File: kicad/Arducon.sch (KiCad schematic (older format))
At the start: 75 parts, among them J101 To Radio, J102 DB9 Female, J103 To Antenna, J104 Conn_01x08, J105 Conn_01x08, J106 Logic Level, J107 External Power Source, J108 Controlled Power, J109 Conn_01x01, J110 Conn_01x01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

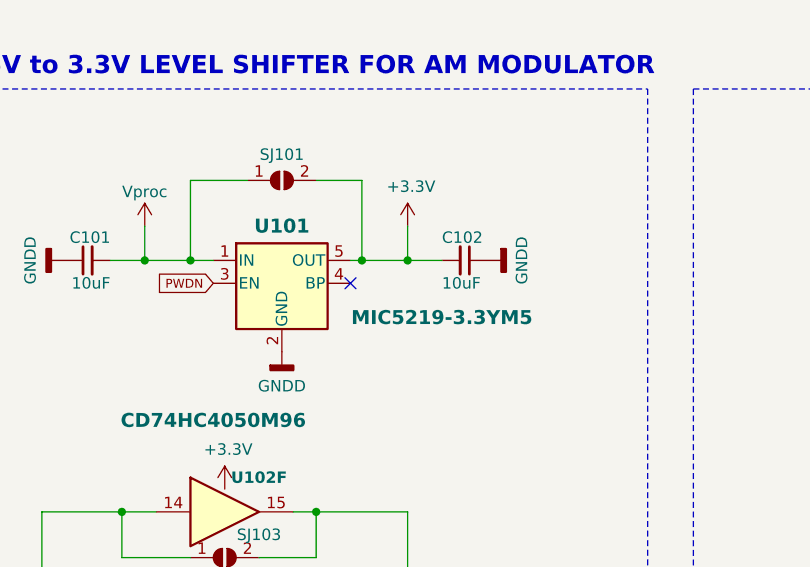
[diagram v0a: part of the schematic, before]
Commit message: PCB Design Updates
Updates for manufacturability. Expanded BOM information items.
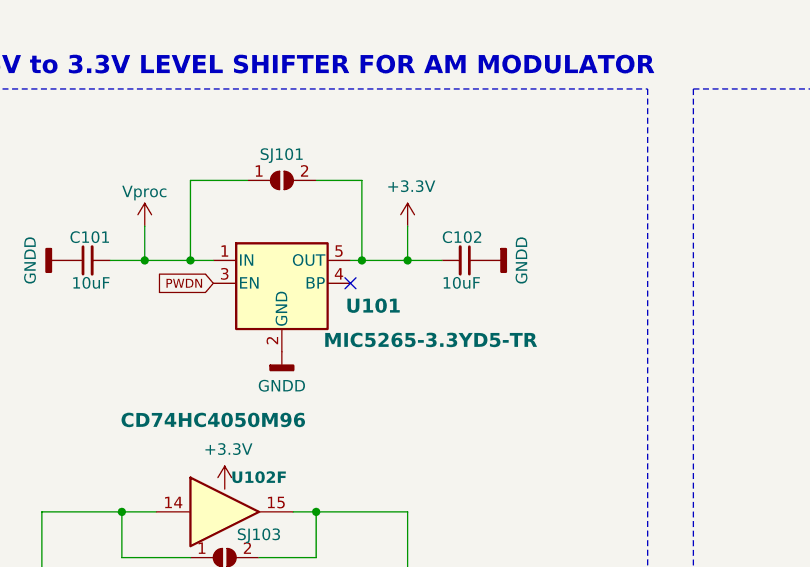
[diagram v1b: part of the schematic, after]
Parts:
- C101, C102, C104: LCSC Part Number (none) -> C15850
- C103, C108, C109, C110: LCSC Part Number (none) -> C476766
- D101, D108, D109: value MSS1P4-M3_89A -> MSS1P2L-M3/89A; Description DIODE SCHOTTKY 40V 1A MICROSMP -> DIODE SCHOTTKY 20V 1A MICROSMP; LCSC Part Number (none) -> C506621; Link <a href=\"https://www.digikey.com/products/en?keywords=MSS1P4-M3/89AGICT-ND\">Link</a> -> <a href=\"https://www.digikey.com/products/en?keywords=MSS1P2L-M3/89AGICT-ND\">Link</a>; Manufacturer PN MSS1P4-M3/89A -> MSS1P2L-M3/89A; Part No. MSS1P4-M3/89AGICT-ND -> MSS1P2L-M3/89AGICT-ND
- D102: LCSC Part Number (none) -> C389523
- D103, D104, D105, D106, D107: LCSC Part Number (none) -> C316054
- FB101, FB102, FB103, FB104, FB105, FB106: LCSC Part Number (none) -> C96697
- Q101, Q103, Q104: LCSC Part Number (none) -> C181121
- Q102: value LMN400E01 -> LMN200; Description MCU LOAD SWITCH 400MA SOT-363 -> MCU LOAD SWITCH 200MA SOT-363; LCSC Part Number (none) -> C150757; Link <a href=\"https://www.digikey.com/products/en?keywords=LMN4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 -> <a href=\"https://www.digikey.com/products/en?keywords=LMN2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; Manufacturer PN LMN400E01-7 -> LMN200B02-7; Part No. LMN400E01DICT-ND -> LMN200B02DICT-ND
- R101, R106: LCSC Part Number (none) -> C96346
- R102: LCSC Part Number (none) -> C114561
- R103, R104, R108, R109, R111, R112: LCSC Part Number (none) -> C17414
- R105: LCSC Part Number (none) -> C107700
- R107: LCSC Part Number (none) -> C416820
- R110: LCSC Part Number (none) -> C193989
- R113: LCSC Part Number (none) -> C170839
- R114: LCSC Part Number (none) -> C328396
- RV101: LCSC Part Number (none) -> C719176
- SW101: LCSC Part Number (none) -> C221877; Manufacturer PN PTS645SL50SMTR92 LFS -> PTS645SL50SMTR92LFS
- SW102: LCSC Part Number (none) -> C221841
- U101: value MIC5219-3.3YM5 -> MIC5265-3.3YD5-TR; Description IC REG LINEAR 3.3V 500MA SOT23-5 -> IC REG LINEAR 3.3V 150MA SOT23-5; LCSC Part Number (none) -> C37970; Link <a href=\"https://www.digikey.com/products/en?keywords=576-1281-1-ND \">Link</a> -> <a href=\"https://www.digikey.com/products/en?keywords=576-2835-1-ND\">Link</a>; Manufacturer PN MIC5219-3.3YM5-TR -> MIC5265-3.3YD5-TR; Part No. 576-1281-1-ND -> 576-2835-1-ND
- U102: LCSC Part Number (none) -> C131932
- U104: value F1975 -> F1975NCGI; LCSC Part Number (none) -> C1525854

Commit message: Schematic Update
Changed schematic and PCB design to support two different RTC devices: DS3132 and RV-8803-C7. Only one RTC option should be populated.
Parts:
- removed R112: 10k, Resistors_SMD:R_0805, symbol Device:R
- removed U103: RV-3028-C7, Oddities:RV-3028-C7, symbol Timer_RTC:RV-3028-C7
- added C105: 10uF, Capacitors_SMD:C_0805, symbol Device:C_Small
- added U103: RV-8803-C7, Oddities:RV-3028-C7, symbol Timer_RTC:RV-8803-C7
- added U105: DS3231, SMD_Packages:SO16, symbol Timer_RTC:DS3231M
- BT101: Digi-Key Part No. (none) -> BC501SM-ND; Part No. BC501SM-ND -> (none)
- C101, C102, C104: Digi-Key Part No. (none) -> 490-5523-1-ND; Part No. 490-5523-1-ND -> (none)
- C103, C108, C109, C110: Digi-Key Part No. (none) -> 478-1395-1-ND; Part No. 478-1395-1-ND -> (none)
- D101, D108, D109: Digi-Key Part No. (none) -> MSS1P2L-M3/89AGICT-ND; Part No. MSS1P2L-M3/89AGICT-ND -> (none)
- D102: Digi-Key Part No. (none) -> 732-4984-1-ND; Part No. 732-4984-1-ND -> (none)
- D103, D104, D105, D106, D107: Digi-Key Part No. (none) -> CG0603MLC-05LECT-ND; Part No. CG0603MLC-05LECT-ND -> (none)
- FB101, FB102, FB103, FB104, FB105, FB106: Digi-Key Part No. (none) -> 240-2377-1-ND; Part No. 240-2377-1-ND -> (none)
- J101, J103, J113: Digi-Key Part No. (none) -> CON-SMA-EDGE-S-ND; Part No. CON-SMA-EDGE-S-ND -> (none)
- J102: Description TBD -> (none); Digi-Key Part No. (none) -> 609-1525-ND; Manufacturer TBD -> TH; Manufacturer PN TBD -> TH; Part No. 609-1525-ND -> (none)
- J104, J105, J106, J107, J108, J109, J110, SJ101, SJ102, SJ103, SJ104, SJ105, SJ106, SJ107, SJ108, SJ110, TP101, W101, W102: Digi-Key Part No. (none) -> np; Part No. np -> (none)
- J111: Description TBD -> (none); Digi-Key Part No. (none) -> 609-5908-ND; Manufacturer TBD -> TH; Manufacturer PN TBD -> TH; Part No. 609-5908-ND -> (none)
- J112: Description TBD -> (none); Digi-Key Part No. (none) -> 929550-01-06-ND; Manufacturer TBD -> TH; Manufacturer PN TBD -> TH; Part No. 929550-01-06-ND -> (none)
- MOD101: Digi-Key Part No. (none) -> 1568-1055-ND; Part No. 1568-1055-ND -> (none)
- P101: Description TBD -> (none); Digi-Key Part No. (none) -> 609-3487-1-ND; Manufacturer TBD -> np; Manufacturer PN TBD -> np; Part No. 609-3487-1-ND -> (none)
- Q101, Q103, Q104: Digi-Key Part No. (none) -> MMBT2222ATPMSCT-ND; Part No. MMBT2222ATPMSCT-ND -> (none)
- Q102: Digi-Key Part No. (none) -> LMN200B02DICT-ND; Part No. LMN200B02DICT-ND -> (none)
- R101, R106: Digi-Key Part No. (none) -> 311-100KCRCT-ND; Part No. 311-100KCRCT-ND -> (none)
- R102: Digi-Key Part No. (none) -> 311-2.20KCRCT-ND; Part No. 311-2.20KCRCT-ND -> (none)
- R103, R104, R108, R109, R111: Digi-Key Part No. (none) -> 311-10.0KCRCT-ND; Part No. 311-10.0KCRCT-ND -> (none)
- R105: Digi-Key Part No. (none) -> RMCF0805FT1M00CT-ND; Part No. RMCF0805FT1M00CT-ND -> (none)
- R107: Digi-Key Part No. (none) -> 311-162KCRCT-ND; Part No. 311-162KCRCT-ND -> (none)
- R110: Digi-Key Part No. (none) -> 311-10.0CRCT-ND; Part No. 311-10.0CRCT-ND -> (none)
- R113: Digi-Key Part No. (none) -> 311-210KCRCT-ND; Part No. 311-210KCRCT-ND -> (none)
- R114: Digi-Key Part No. (none) -> 311-470CRCT-ND; Part No. 311-470CRCT-ND -> (none)
- RV101: Digi-Key Part No. (none) -> TC33X-103ECT-ND; Part No. TC33X-103ECT-ND -> (none)
- SW101: Digi-Key Part No. (none) -> CKN9088CT-ND; Part No. CKN9088CT-ND -> (none)
- SW102: Digi-Key Part No. (none) -> 401-2016-1-ND; Part No. 401-2016-1-ND -> (none)
- U101: Digi-Key Part No. (none) -> 576-2835-1-ND; Part No. 576-2835-1-ND -> (none)
- U102: Digi-Key Part No. (none) -> 296-14529-1-ND; Part No. 296-14529-1-ND -> (none)
- U104: Digi-Key Part No. (none) -> 800-3576-ND; Part No. 800-3576-ND -> (none)
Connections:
- wire segments 325 -> 335
- no-connect marks 17 -> 19
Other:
- note added: "Real-Time Clock\n(Select only one of two device configurations)"
- note removed: "Real-Time Clock"
- moved on the sheet: BT101, C103, C104, C108, C109, D102, D103, D104, D105, D106, D107, FB101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

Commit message: Moved CLKOE to Vproc
o Corrected CLKOE to have a pull-up instead of a pull-down.
o Updated schematic and PCB
o Deleted old BOMs
o Updated new BOMS
o Rebuilt Gerbers and footprint position file
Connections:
- wire segments 335 -> 334
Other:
- moved on the sheet: R111
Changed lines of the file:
@@
 L Device:R R111
 U 1 1 604113C9
-P 9800 9650
-F 0 "R111" H 9900 9800 50  0000 C CNN
-F 1 "10k" V 9700 9650 50  0000 C CNN
-F 2 "Resistors_SMD:R_0805" H 9730 9650 50  0001 C CNN
-F 3 "" H 9800 9650 50  0001 C CNN
-F 4 "311-10.0KCRCT-ND" H 9800 9650 60  0001 C CNN "Digi-Key Part No."
-F 5 "<a href=\"https://www.digikey.com/products/en?keywords=311-10.0KCRCT-ND\">Link</a>" H 9800 9650 60  0001 C CNN "Link"
-F 6 "Yageo" H 9800 9650 50  0001 C CNN "Manufacturer"
-F 7 "RC0805FR-0710KL" H 9800 9650 50  0001 C CNN "Manufacturer PN"
-F 8 "RES SMD 10K OHM 1% 1/8W 0805" H 9800 9650 50  0001 C CNN "Description"
-F 9 "C17414" H 9800 9650 50  0001 C CNN "LCSC Part Number"
-	1    9800 9650
-	1    0    0    -1
-$EndComp
-$Comp
-L power:GNDD #PWR0121
-U 1 1 60412D90
-P 9800 9800
-F 0 "#PWR0121" H 9800 9550 50  0001 C CNN
-F 1 "GNDD" H 9800 9650 50  0000 C CNN
-F 2 "" H 9800 9800 50  0000 C CNN
-F 3 "" H 9800 9800 50  0000 C CNN
-	1    9800 9800
-	1    0    0    -1
-$EndComp
-Wire Wire Line
-	9650 9450 9800 9450
-Wire Wire Line
-	9800 9450 9800 9500
+P 9950 9300
+F 0 "R111" H 10150 9300 50  0000 C CNN
+F 1 "10k" V 9850 9300 50  0000 C CNN
+F 2 "Resistors_SMD:R_0805" H 9880 9300 50  0001 C CNN
+F 3 "" H 9950 9300 50  0001 C CNN
+F 4 "311-10.0KCRCT-ND" H 9950 9300 60  0001 C CNN "Digi-Key Part No."
+F 5 "<a href=\"https://www.digikey.com/products/en?keywords=311-10.0KCRCT-ND\">Link</a>" H 9950 9300 60  0001 C CNN "Link"
+F 6 "Yageo" H 9950 9300 50  0001 C CNN "Manufacturer"
+F 7 "RC0805FR-0710KL" H 9950 9300 50  0001 C CNN "Manufacturer PN"
+F 8 "RES SMD 10K OHM 1% 1/8W 0805" H 9950 9300 50  0001 C CNN "Description"
+F 9 "C17414" H 9950 9300 50  0001 C CNN "LCSC Part Number"
+	1    9950 9300
+	-1   0    0    1
+$EndComp
+Wire Wire Line
+	9650 9450 9950 9450
 $Comp
 L power:PWR_FLAG #FLG0104
@@
 Wire Notes Line
 	10650 7650 10650 10300
+$Comp
+L power:Vproc #PWR0121
+U 1 1 6099BDD9
+P 9950 9150
+F 0 "#PWR0121" H 9950 9000 50  0001 C CNN
+F 1 "Vproc" H 9950 9300 50  0000 C CNN
+F 2 "" H 9950 9150 50  0000 C CNN
+F 3 "" H 9950 9150 50  0000 C CNN
+	1    9950 9150
+	1    0    0    -1
+$EndComp
 Wire Bus Line
 	6150 4000 6150 6700

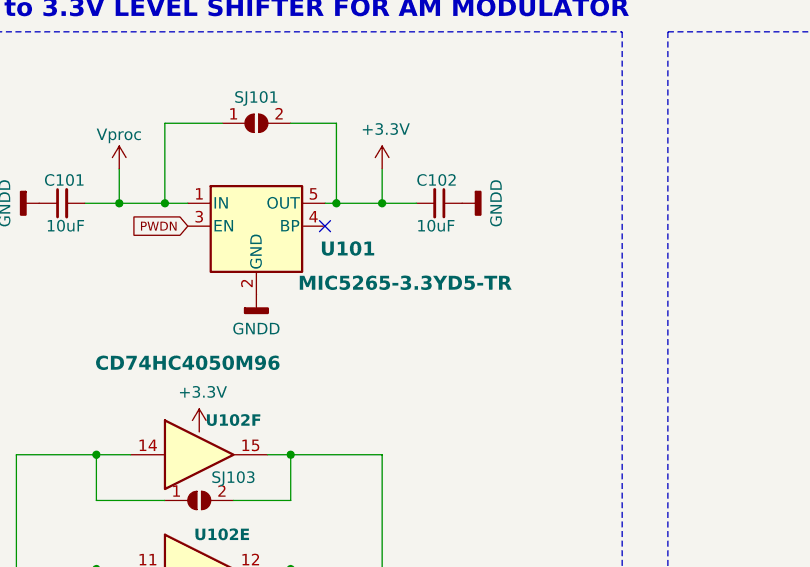
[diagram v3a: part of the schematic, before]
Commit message: BOM Update
Specified a different regulator chip
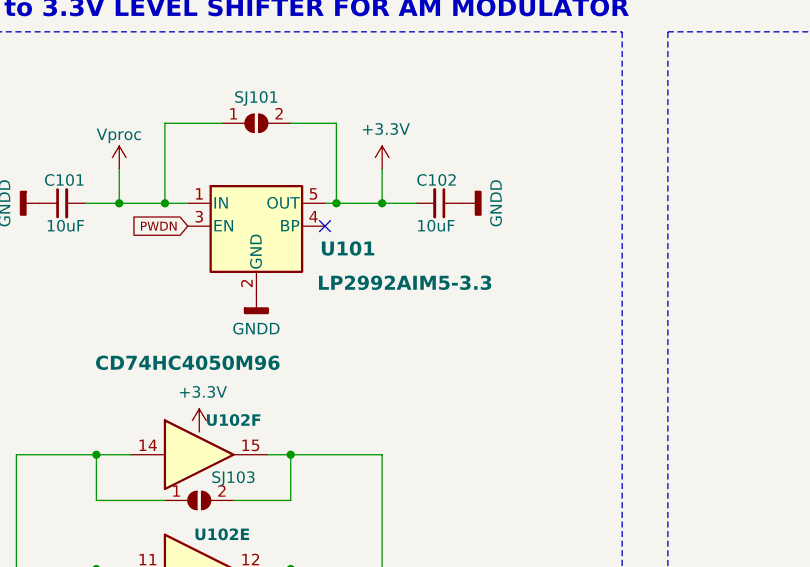
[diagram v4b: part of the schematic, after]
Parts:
- SW101: value SPST_small -> SPST
- U101: value MIC5265-3.3YD5-TR -> LP2992AIM5-3.3; Description IC REG LINEAR 3.3V 150MA SOT23-5 -> IC REG LINEAR 3.3V 250MA SOT23-5; Digi-Key Part No. 576-2835-1-ND -> LP2992AIM5-3.3/NOPBCT-ND; Link <a href=\"https://www.digikey.com/products/en?keywords=576-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 -> <a href=\"https://www.digikey.com/products/en?keywords=LP29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; Manufacturer Microchip Technology -> Texas Instruments; Manufacturer PN MIC5265-3.3YD5-TR -> LP2992AIM5-3.3/NOPB
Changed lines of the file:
@@
 P 7250 5600
 F 0 "SW101" H 7250 5500 50  0000 C CNN
-F 1 "SPST_small" H 7250 5500 50  0001 C CNN
+F 1 "SPST" H 7250 5500 50  0001 C CNN
 F 2 "Buttons_Switches_SMD:PTS645SL50SMTR92" H 7250 5600 50  0001 C CNN
 F 3 "" H 7250 5600 50  0001 C CNN
@@
 P 10350 1700
 F 0 "U101" H 10750 1600 61  0000 C CNB
-F 1 "MIC5265-3.3YD5-TR" H 11000 1450 61  0000 C CNB
+F 1 "LP2992AIM5-3.3" H 11000 1450 61  0000 C CNB
 F 2 "TO_SOT_Packages_SMD:SOT-23-5" H 10350 2025 50  0001 C CNN
 F 3 "" H 10350 1700 50  0001 C CNN
-F 4 "576-2835-1-ND" H 10350 1700 50  0001 C CNN "Digi-Key Part No."
-F 5 "<a href=\"https://www.digikey.com/products/en?keywords=576-2835-1-ND\">Link</a>" H 10350 1700 50  0001 C CNN "Link"
-F 6 "Microchip Technology" H 10350 1700 50  0001 C CNN "Manufacturer"
-F 7 "MIC5265-3.3YD5-TR" H 10350 1700 50  0001 C CNN "Manufacturer PN"
-F 8 "IC REG LINEAR 3.3V 150MA SOT23-5" H 10350 1700 50  0001 C CNN "Description"
+F 4 "LP2992AIM5-3.3/NOPBCT-ND" H 10350 1700 50  0001 C CNN "Digi-Key Part No."
+F 5 "<a href=\"https://www.digikey.com/products/en?keywords=LP2992AIM5-3.3/NOPBCT-ND\">Link</a>" H 10350 1700 50  0001 C CNN "Link"
+F 6 "Texas Instruments" H 10350 1700 50  0001 C CNN "Manufacturer"
+F 7 "LP2992AIM5-3.3/NOPB" H 10350 1700 50  0001 C CNN "Manufacturer PN"
+F 8 "IC REG LINEAR 3.3V 250MA SOT23-5" H 10350 1700 50  0001 C CNN "Description"
 F 9 "C37970" H 10350 1700 50  0001 C CNN "LCSC Part Number"
 	1    10350 1700

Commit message: Minor Updates
Minor updates for PCB files in anticipation of small build order.
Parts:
- BT101: symbol Device:Battery_Single_Cell -> Arducon-rescue:Battery_Single_Cell-Device
- D101, D108, D109: symbol Diode:MSS1P4-M3_89A -> Arducon-rescue:MSS1P4-M3_89A-Diode
- MOD101: symbol MCU_Module:Arduino_Pro_Mini-MCU_Module -> Arducon-rescue:Arduino_Pro_Mini-MCU_Module-MCU_Module
- Q101, Q103, Q104: symbol Transistor_BJT:PN2222A -> Arducon-rescue:PN2222A-Transistor_BJT
- Q102: symbol Power_Protection:LMN200B01 -> Arducon-rescue:LMN200B01-Power_Protection
- SW101: symbol Switch:SPST_small -> Arducon-rescue:SPST_small-Switch
- U102: symbol Logic_LevelTranslator:CD74HC4050M96-74xx -> Arducon-rescue:CD74HC4050M96-74xx-Logic_LevelTranslator
- U103: symbol Timer_RTC:RV-8803-C7 -> Arducon-rescue:RV-8803-C7-Timer_RTC
- U104: symbol RF:F1975NCGI -> Arducon-rescue:F1975NCGI-RF
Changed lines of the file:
@@
 $EndComp
 $Comp
-L power:Vproc #PWR0127
+L Arducon-rescue:Vproc-power #PWR0127
 U 1 1 591CAC09
 P 3800 3700
@@
 $EndComp
 $Comp
-L power:Vproc #PWR0107
+L Arducon-rescue:Vproc-power #PWR0107
 U 1 1 5AB7DABB
 P 9250 8150
@@
 $EndComp
 $Comp
-L Device:Battery_Single_Cell BT101
+L Arducon-rescue:Battery_Single_Cell-Device BT101
 U 1 1 5BCD438E
 P 6550 8100
@@
 $EndComp
 $Comp
-L power:Vproc #PWR0144
+L Arducon-rescue:Vproc-power #PWR0144
 U 1 1 5C60DF91
 P 5200 7150
@@
 $EndComp
 $Comp
-L Switch:SPST_small SW101
+L Arducon-rescue:SPST_small-Switch SW101
 U 1 1 5F9DCC49
 P 7250 5600
@@
 $EndComp
 $Comp
-L MCU_Module:Arduino_Pro_Mini-MCU_Module MOD101
+L Arducon-rescue:Arduino_Pro_Mini-MCU_Module-MCU_Module MOD101
 U 1 1 5FC82DF4
 P 4950 5300
@@
 $EndComp
 $Comp
-L power:Vproc #PWR0134
+L Arducon-rescue:Vproc-power #PWR0134
 U 1 1 5FF2E22F
 P 2950 3550
@@
 	3700 6500 3750 6500
 $Comp
-L RF:F1975NCGI U104
+L Arducon-rescue:F1975NCGI-RF U104
 U 1 1 5FF7DEC4
 P 14100 2800
@@
 $EndComp
 $Comp
-L Logic_LevelTranslator:CD74HC4050M96-74xx U102
+L Arducon-rescue:CD74HC4050M96-74xx-Logic_LevelTranslator U102
 U 1 1 5FFA3B6A
 P 10100 5250
@@
 $EndComp
 $Comp
-L Logic_LevelTranslator:CD74HC4050M96-74xx U102
+L Arducon-rescue:CD74HC4050M96-74xx-Logic_LevelTranslator U102
 U 2 1 5FFA7F9B
 P 10100 4700
@@
 $EndComp
 $Comp
-L Logic_LevelTranslator:CD74HC4050M96-74xx U102
+L Arducon-rescue:CD74HC4050M96-74xx-Logic_LevelTranslator U102
 U 3 1 5FFA8DF3
 P 10100 4150
@@
 $EndComp
 $Comp
-L Logic_LevelTranslator:CD74HC4050M96-74xx U102
+L Arducon-rescue:CD74HC4050M96-74xx-Logic_LevelTranslator U102
 U 4 1 5FFA9DCC
 P 10100 3700
@@
 $EndComp
 $Comp
-L Logic_LevelTranslator:CD74HC4050M96-74xx U102
+L Arducon-rescue:CD74HC4050M96-74xx-Logic_LevelTranslator U102
 U 5 1 5FFAB336
 P 10100 3200
@@
 $EndComp
 $Comp
-L Logic_LevelTranslator:CD74HC4050M96-74xx U102
+L Arducon-rescue:CD74HC4050M96-74xx-Logic_LevelTranslator U102
 U 6 1 5FFAC3C8
 P 10100 2700
@@
 	3850 2600 3850 2500
 $Comp
-L Power_Protection:LMN200B01 Q102
+L Arducon-rescue:LMN200B01-Power_Protection Q102
 U 1 1 5FC59E4B
 P 13550 7600
@@
 $EndComp
 $Comp
-L power:Vproc #PWR0113
+L Arducon-rescue:Vproc-power #PWR0113
 U 1 1 5FFE7858
 P 9750 1450
@@
 NoConn ~ 4050 5000
 $Comp
-L power:Vproc #PWR0156
+L Arducon-rescue:Vproc-power #PWR0156
 U 1 1 5FDC95A5
 P 2750 1950
@@
 $EndComp
 $Comp
-L Transistor_BJT:PN2222A Q101
+L Arducon-rescue:PN2222A-Transistor_BJT Q101
 U 1 1 603D3C3C
 P 3950 2800
@@
 $EndComp
 $Comp
-L Diode:MSS1P4-M3_89A D109
+L Arducon-rescue:MSS1P4-M3_89A-Diode D109
 U 1 1 6037BF00
 P 7850 8100
@@
 $EndComp
 $Comp
-L Transistor_BJT:PN2222A Q103
+L Arducon-rescue:PN2222A-Transistor_BJT Q103
 U 1 1 6037AAF1
 P 1900 5300
@@
 	6400 6100 6250 6100
 $Comp
-L Transistor_BJT:PN2222A Q104
+L Arducon-rescue:PN2222A-Transistor_BJT Q104
 U 1 1 6041235C
 P 8350 9400
@@
 $EndComp
 $Comp
-L power:Vproc #PWR0160
+L Arducon-rescue:Vproc-power #PWR0160
 U 1 1 606F1DF4
 P 7300 4700
@@
 	3750 6500 4050 6500
 $Comp
-L Diode:MSS1P4-M3_89A D108
+L Arducon-rescue:MSS1P4-M3_89A-Diode D108
 U 1 1 609D6090
 P 9250 8300
@@
 $EndComp
 $Comp
-L Diode:MSS1P4-M3_89A D101
+L Arducon-rescue:MSS1P4-M3_89A-Diode D101
 U 1 1 609FC00E
 P 3550 6500
@@
 $EndComp
 $Comp
-L power:Vproc #PWR0128
+L Arducon-rescue:Vproc-power #PWR0128
 U 1 1 60D66070
 P 6900 8900
@@
 NoConn ~ 7500 9350
 $Comp
-L Timer_RTC:RV-8803-C7 U103
+L Arducon-rescue:RV-8803-C7-Timer_RTC U103
 U 1 1 60FCCE49
 P 9250 9300
@@
 	10650 7650 10650 10300
 $Comp
-L power:Vproc #PWR0121
+L Arducon-rescue:Vproc-power #PWR0121
 U 1 1 6099BDD9
 P 9950 9150

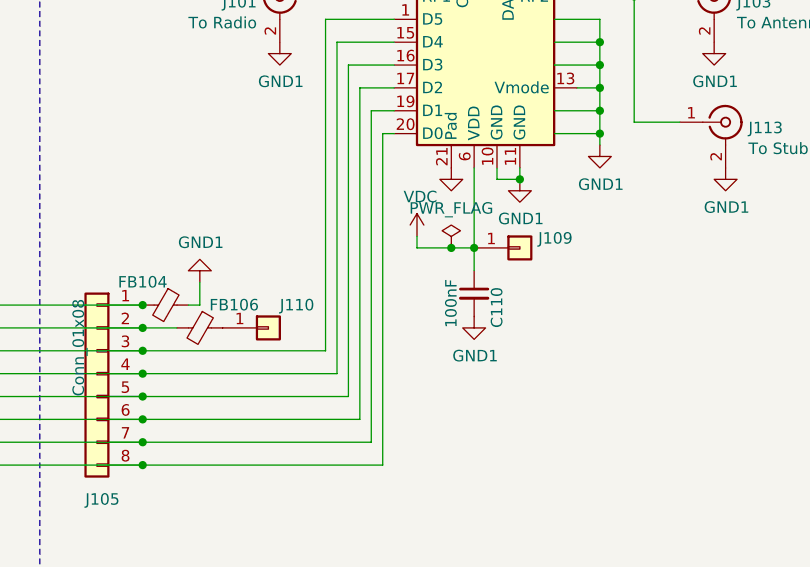
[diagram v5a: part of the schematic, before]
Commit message: PCB Updates
o Removed +V jumper wire from attenuator board
o Fixed ground thermal relief around stub filter xmsn line
o General routing and stitching via improvements
o Regenerated all Gerber and production files
o Regenerated BOM
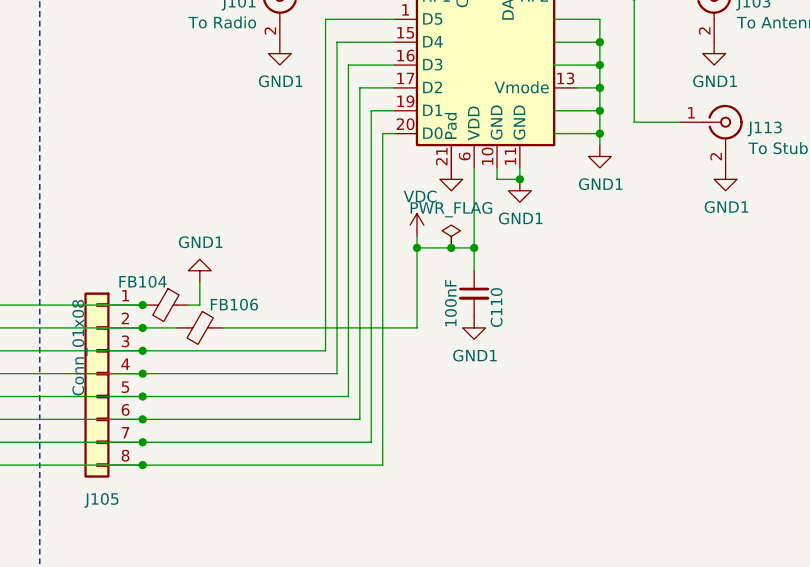
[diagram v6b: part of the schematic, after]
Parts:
- removed J109, J110: Conn_01x01, Pin_Headers:Pin_Header_Straight_1x01, symbol Connector_Generic:Conn_01x01
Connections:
- net VDC: now also FB106.1
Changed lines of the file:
@@
 Wire Wire Line
 	13650 3150 13700 3150
-$Comp
-L Connector_Generic:Conn_01x01 J109
-U 1 1 6011CEB1
-P 14250 3650
-F 0 "J109" H 14330 3692 50  0000 L CNN
-F 1 "Conn_01x01" H 14330 3601 50  0001 L CNN
-F 2 "Pin_Headers:Pin_Header_Straight_1x01" H 14250 3650 50  0001 C CNN
-F 3 "" H 14250 3650 50  0001 C CNN
-F 4 "np" H 14250 3650 50  0001 C CNN "Digi-Key Part No."
-F 5 "np" H 14250 3650 50  0001 C CNN "Link"
-	1    14250 3650
-	1    0    0    -1
-$EndComp
-$Comp
-L Connector_Generic:Conn_01x01 J110
-U 1 1 60130A78
-P 13150 4000
-F 0 "J110" H 13200 4100 50  0000 L CNN
-F 1 "Conn_01x01" H 13230 3951 50  0001 L CNN
-F 2 "Pin_Headers:Pin_Header_Straight_1x01" H 13150 4000 50  0001 C CNN
-F 3 "" H 13150 4000 50  0001 C CNN
-F 4 "np" H 13150 4000 50  0001 C CNN "Digi-Key Part No."
-F 5 "np" H 13150 4000 50  0001 C CNN "Link"
-	1    13150 4000
-	1    0    0    -1
-$EndComp
 Wire Wire Line
 	14050 3750 14050 3650
@@
 	1    0    0    -1
 $EndComp
+Wire Wire Line
+	12950 4000 13800 4000
+Wire Wire Line
+	13800 4000 13800 3650
 Wire Bus Line
 	6150 4000 6150 6700
+Connection ~ 13800 3650
 $EndSCHEMATC
